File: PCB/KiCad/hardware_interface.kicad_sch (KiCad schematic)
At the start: 5 parts

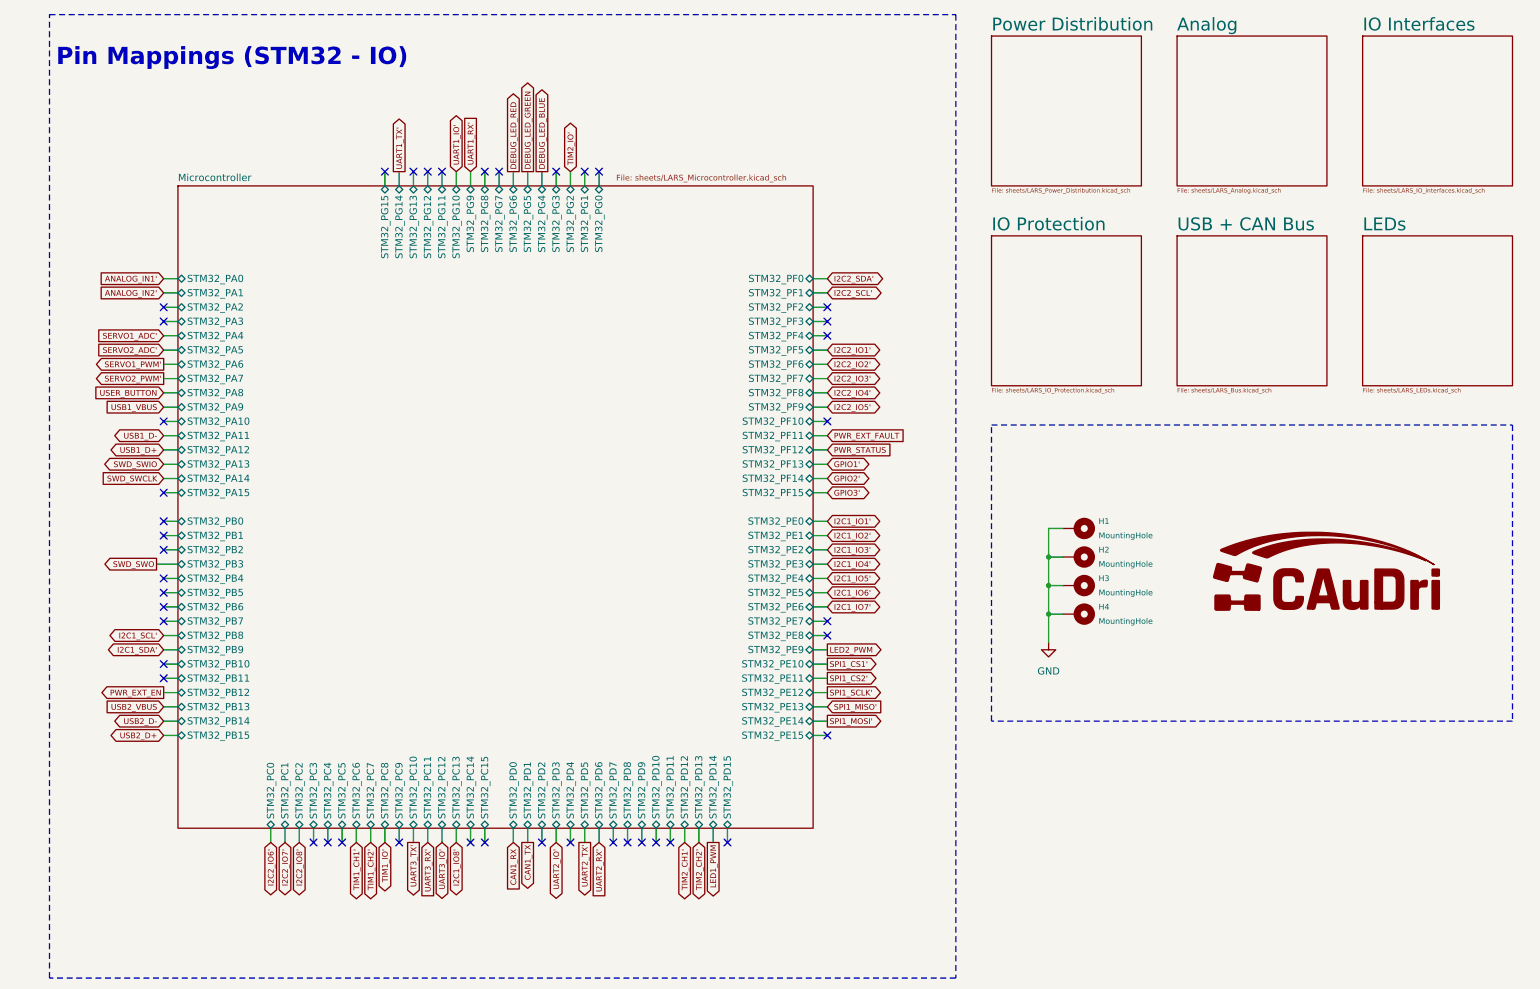
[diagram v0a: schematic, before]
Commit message: PCB: add XOR gate for RC Receiver
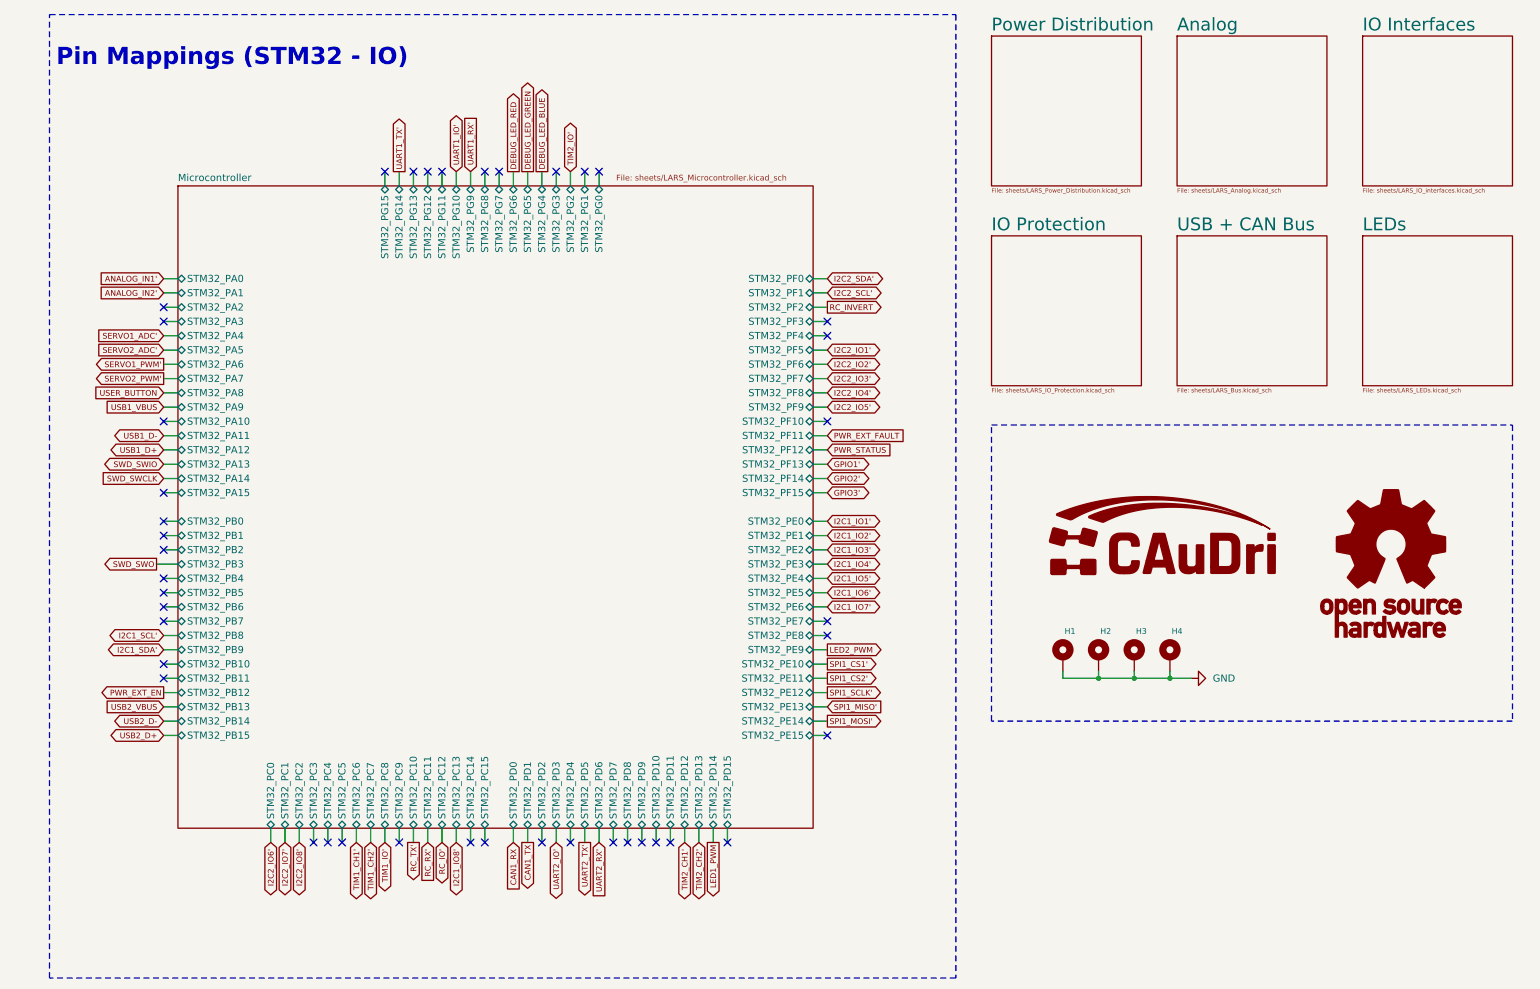
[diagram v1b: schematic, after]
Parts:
- added G2: OSHWA Logo, LARS_Hardware_Interface:OSHWA Logo, symbol LARS_Hardware_Interface:OSHWA Logo
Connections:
- no-connect marks 43 -> 42
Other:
- moved on the sheet: H1, H2, H3, H4
